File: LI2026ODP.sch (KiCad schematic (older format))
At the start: 34 parts, among them J1 9-1437539-2, J2 Conn_01x05_Male, U1 LM2936MM-3.3, U2 STM32G0B1KET6, U3 max6921aui

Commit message: Modify the U2 Footprint.
 Issue : #5

 The footprint was incorrect. Substitute it with the right 0.8mm pitch one.
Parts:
- U2: footprint STM32G0B1:STM32G0B1KET6 -> Package_QFP:LQFP-32_7x7mm_P0.8mm
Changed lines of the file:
@@
 F 0 "U2" H 3150 3087 60  0000 C CNN
 F 1 "STM32G0B1KET6" H 3150 2981 60  0000 C CNN
-F 2 "STM32G0B1:STM32G0B1KET6" H 3150 2940 60  0001 C CNN
+F 2 "Package_QFP:LQFP-32_7x7mm_P0.8mm" H 3150 2940 60  0001 C CNN
 F 3 "" H 1650 2600 60  0000 C CNN
 	1    1650 2600
@@
 F 0 "U2" H 4550 5850 60  0000 L CNN
 F 1 "STM32G0B1KET6" H 4550 5750 60  0000 L CNN
-F 2 "STM32G0B1:STM32G0B1KET6" H 5550 5840 60  0001 C CNN
+F 2 "Package_QFP:LQFP-32_7x7mm_P0.8mm" H 5550 5840 60  0001 C CNN
 F 3 "" H 4050 5500 60  0000 C CNN
 	2    4050 5500

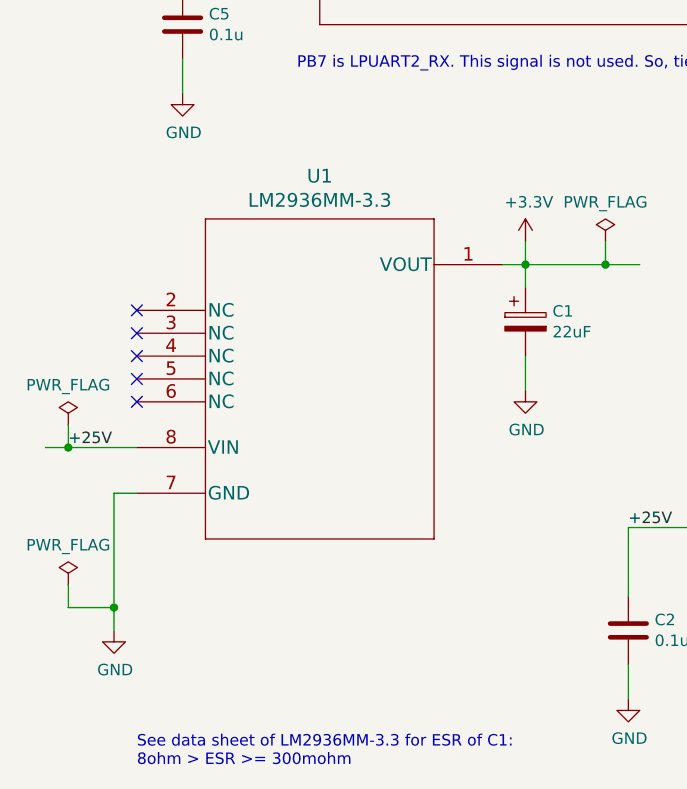
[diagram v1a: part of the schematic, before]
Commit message: Add capacitor for 25v line
 Issue #8 .

 Add C6 close to the voltage regulator.
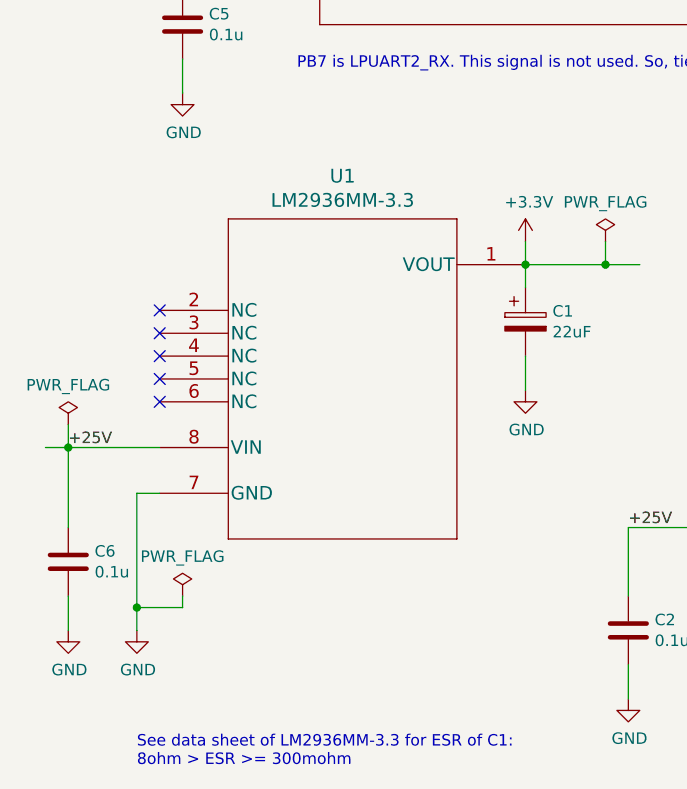
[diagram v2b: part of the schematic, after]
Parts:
- added C6: 0.1u, Capacitor_SMD:C_0603_1608Metric_Pad1.08x0.95mm_HandSolder, symbol Device:C
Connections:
- wire segments 145 -> 146
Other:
- moved on the sheet: U1
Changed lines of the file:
@@
 L power:GND #PWR015
 U 1 1 61F0F6A5
-P 1050 7050
-F 0 "#PWR015" H 1050 6800 50  0001 C CNN
-F 1 "GND" H 1055 6877 50  0000 C CNN
-F 2 "" H 1050 7050 50  0001 C CNN
-F 3 "" H 1050 7050 50  0001 C CNN
-	1    1050 7050
+P 1150 7050
+F 0 "#PWR015" H 1150 6800 50  0001 C CNN
+F 1 "GND" H 1155 6877 50  0000 C CNN
+F 2 "" H 1150 7050 50  0001 C CNN
+F 3 "" H 1150 7050 50  0001 C CNN
+	1    1150 7050
 	1    0    0    -1
 $EndComp
@@
 L power:PWR_FLAG #FLG0103
 U 1 1 62159FE9
-P 850 6850
-F 0 "#FLG0103" H 850 6925 50  0001 C CNN
-F 1 "PWR_FLAG" H 850 7023 50  0000 C CNN
-F 2 "" H 850 6850 50  0001 C CNN
-F 3 "~" H 850 6850 50  0001 C CNN
-	1    850  6850
-	1    0    0    -1
-$EndComp
-Wire Wire Line
-	850  6850 850  6950
+P 1350 6900
+F 0 "#FLG0103" H 1350 6975 50  0001 C CNN
+F 1 "PWR_FLAG" H 1350 7073 50  0000 C CNN
+F 2 "" H 1350 6900 50  0001 C CNN
+F 3 "~" H 1350 6900 50  0001 C CNN
+	1    1350 6900
+	1    0    0    -1
+$EndComp
+Wire Wire Line
+	1350 6900 1350 6950
 Wire Wire Line
 	3300 1300 3750 1300
@@
 L LM2936MM:LM2936MM-3.3 U1
 U 1 1 61E62025
-P 1150 5650
-F 0 "U1" H 1950 6237 60  0000 C CNN
-F 1 "LM2936MM-3.3" H 1950 6131 60  0000 C CNN
-F 2 "LM2936MM:LM2936MM-3.3" H 1950 6090 60  0001 C CNN
-F 3 "" H 1150 5650 60  0000 C CNN
-	1    1150 5650
+P 1250 5650
+F 0 "U1" H 2050 6237 60  0000 C CNN
+F 1 "LM2936MM-3.3" H 2050 6131 60  0000 C CNN
+F 2 "LM2936MM:LM2936MM-3.3" H 2050 6090 60  0001 C CNN
+F 3 "" H 1250 5650 60  0000 C CNN
+	1    1250 5650
 	1    0    0    -1
 $EndComp
@@
 	850  6250 750  6250
 Wire Wire Line
-	850  6250 1150 6250
-Wire Wire Line
-	1150 6450 1050 6450
-Wire Wire Line
-	1050 6450 1050 6950
+	850  6250 1250 6250
+Wire Wire Line
+	1250 6450 1150 6450
+Wire Wire Line
+	1150 6450 1150 6950
 Wire Wire Line
 	3200 5350 3200 5450
@@
 	2850 5450 2850 5550
 Wire Wire Line
-	2750 5450 2850 5450
-Wire Wire Line
 	2850 5850 2850 6000
-NoConn ~ 1150 5650
-NoConn ~ 1150 5750
-NoConn ~ 1150 5850
-NoConn ~ 1150 5950
-NoConn ~ 1150 6050
+NoConn ~ 1250 5650
+NoConn ~ 1250 5750
+NoConn ~ 1250 5850
+NoConn ~ 1250 5950
+NoConn ~ 1250 6050
 Text Label 1300 3900 0    50   ~ 0
 SWDIO
@@
 	3950 6800 3950 7350
 Wire Wire Line
-	850  6950 1050 6950
-Connection ~ 1050 6950
-Wire Wire Line
-	1050 6950 1050 7050
+	1350 6950 1150 6950
+Connection ~ 1150 6950
+Wire Wire Line
+	1150 6950 1150 7050
 $Comp
 L Device:CP C1
@@
 Text Label 1300 3000 0    50   ~ 0
 BLANK
+$Comp
+L power:GND #PWR024
+U 1 1 61FAC0D5
+P 850 7050
+F 0 "#PWR024" H 850 6800 50  0001 C CNN
+F 1 "GND" H 855 6877 50  0000 C CNN
+F 2 "" H 850 7050 50  0001 C CNN
+F 3 "" H 850 7050 50  0001 C CNN
+	1    850  7050
+	1    0    0    -1
+$EndComp
+$Comp
+L Device:C C6
+U 1 1 61FAC0DB
+P 850 6750
+F 0 "C6" H 965 6796 50  0000 L CNN
+F 1 "0.1u" H 965 6705 50  0000 L CNN
+F 2 "Capacitor_SMD:C_0603_1608Metric_Pad1.08x0.95mm_HandSolder" H 888 6600 50  0001 C CNN
+F 3 "~" H 850 6750 50  0001 C CNN
+	1    850  6750
+	1    0    0    -1
+$EndComp
+Wire Wire Line
+	850  6600 850  6250
+Wire Wire Line
+	850  6900 850  7050
 $EndSCHEMATC
